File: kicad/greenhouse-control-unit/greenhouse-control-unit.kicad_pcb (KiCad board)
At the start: 2 copper layers, 252.1 x 133.3 mm, 28 parts, among them J1 Screw_Terminal_01x02, J10_Buck2 Conn_01x01_Female, J11_Buck2 Conn_01x01_Female, J12_Buck1 Conn_01x01_Female, J13_Buck1 Conn_01x01_Female, J14_Buck2 Conn_01x01_Female, J15_Buck2 Conn_01x01_Female, J16 Screw_Terminal_01x16, J2 Screw_Terminal_01x02, J3 Screw_Terminal_01x02, J4 Screw_Terminal_01x06, J5 Conn_01x03_Male, J6_Buck1 Conn_01x01_Female, J7_Buck1 Conn_01x01_Female, J8 Conn_01x15_Female, J9 Conn_01x15_Female, Q1 IRLB8721PBF, Q2 IRLB8721PBF, Q3 IRLB8721PBF, Q4 IRLB8721PBF, U1 74HC595, U2 74HC595

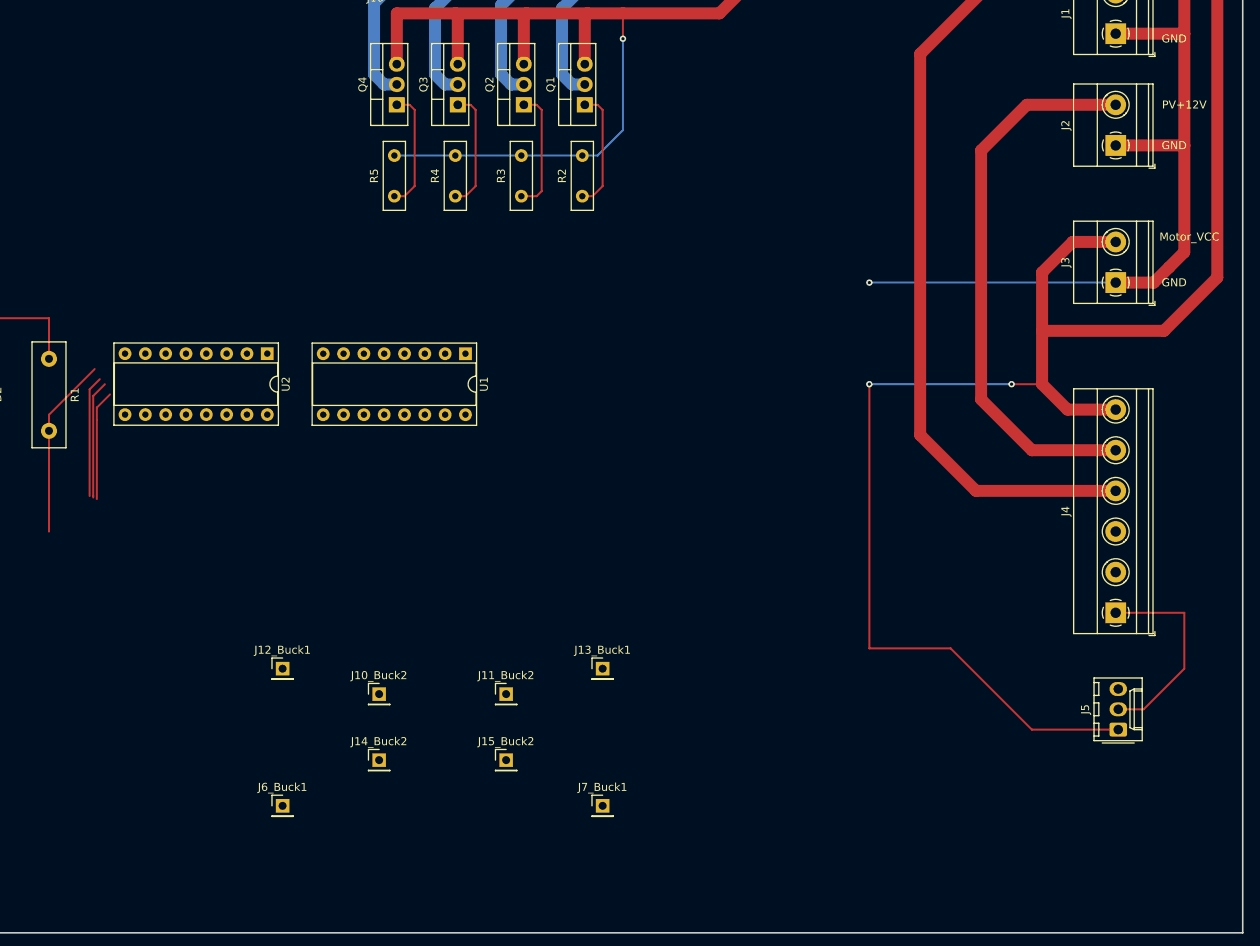
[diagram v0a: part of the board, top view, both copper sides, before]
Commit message: Add SR TTL, FET labels, tie PSU+12V to +12V
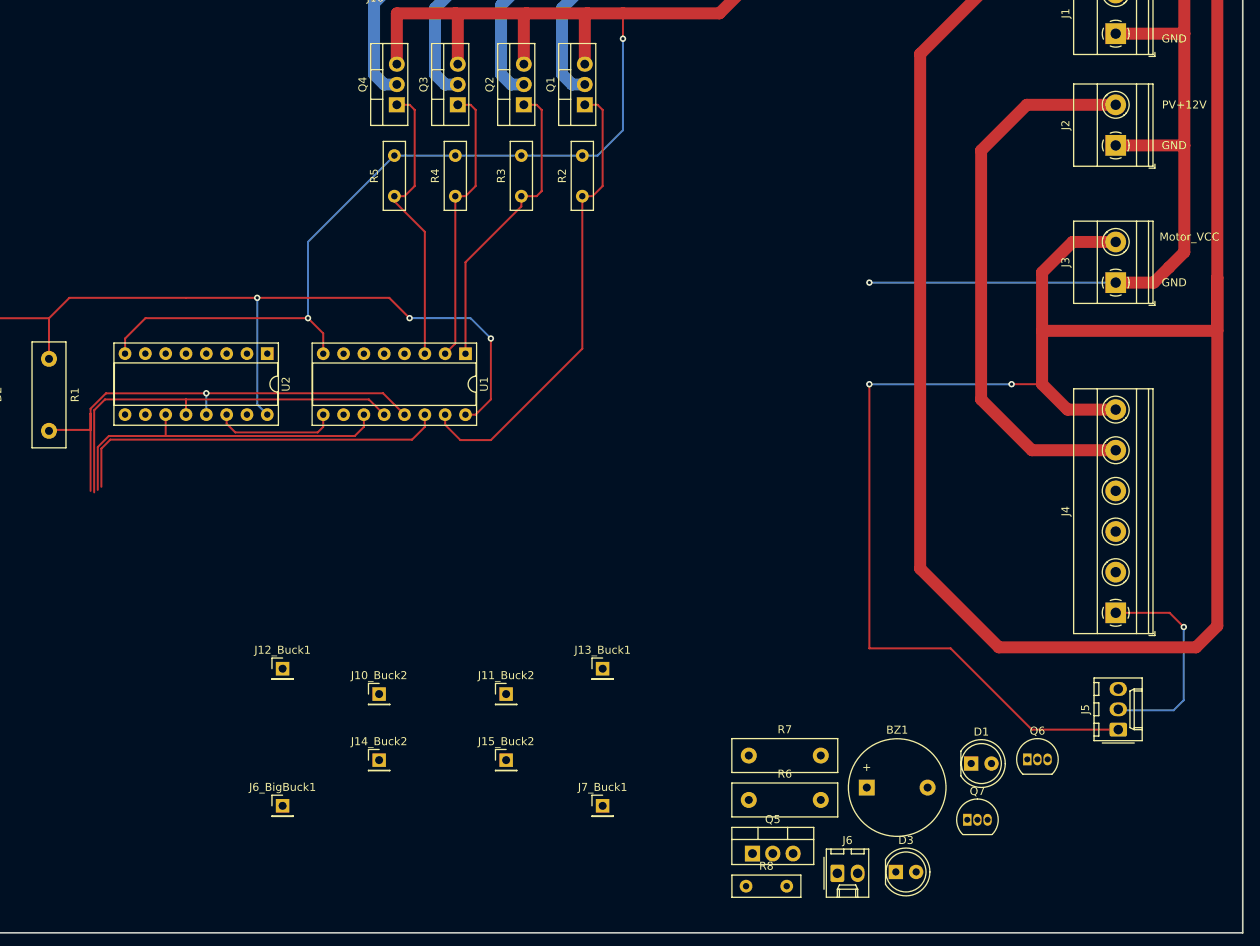
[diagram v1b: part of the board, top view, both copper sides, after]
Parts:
- added BZ1: Buzzer, Buzzer_Beeper:Buzzer_12x9.5RM7.6, F.Cu at (227.3, 137.4)
- added D1: LED, LED_THT:LED_D5.0mm, F.Cu at (240.4, 134.4)
- added D3: LED, LED_THT:LED_D5.0mm, F.Cu at (231.0, 148.0)
- added J6: Conn_01x02_Male, Connector_Molex:Molex_KK-254_AE-6410-02A_1x02_P2.54mm_Vertical, F.Cu at (223.7, 148.1)
- added Q5: IRLB8721PBF, Package_TO_SOT_THT:TO-220-3_Vertical, F.Cu at (213.0, 145.7)
- added Q6: 2N2222A, Package_TO_SOT_THT:TO-92_Inline, F.Cu at (247.4, 133.9)
- added Q7: 2N2222A, Package_TO_SOT_THT:TO-92_Inline, F.Cu at (239.9, 141.4)
- added R6: R4k6, Resistor_THT:R_Box_L13.0mm_W4.0mm_P9.00mm, F.Cu at (212.6, 139.0)
- added R7: R4k6, Resistor_THT:R_Box_L13.0mm_W4.0mm_P9.00mm, F.Cu at (212.6, 133.4)
- added R8: R10k, Resistor_THT:R_Box_L8.4mm_W2.5mm_P5.08mm, F.Cu at (212.2, 149.7)
- renumbered J6_Buck1 to J6_BigBuck1
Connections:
- net /Relay2_IN renamed /ACRelay_IN
- J1 pad 2: /PSU+12V -> +12V
- J4 pad 2: /Relay1_IN -> /FatRelay_Coil
- J4 pad 4: /PSU+12V -> /FatRelay_A
- J9 pad 1: unconnected-(J9-Pad1) -> /MC_D8
- J9 pad 5: /MC_D8 -> unconnected-(J9-Pad5)
- Q1 pad 1: /SR_SW1 -> /SR_SW08
- Q2 pad 1: /SR_SW2 -> /SR_SW09
- Q3 pad 1: /SR_SW3 -> /SR_SW10
- Q4 pad 1: /SR_SW4 -> /SR_SW11
- R2 pad 1: /SR_SW1 -> /SR_SW08
- R3 pad 1: /SR_SW2 -> /SR_SW09
- R4 pad 1: /SR_SW3 -> /SR_SW10
- R5 pad 1: /SR_SW4 -> /SR_SW11
- U1 pad 1: /SR_SW2 -> /StartBeep_SR_SW1
- U1 pad 15: /SR_SW1 -> /FatRelay_SR_SW0
- U1 pad 2: /SR_SW3 -> /CaseFan_SR_SW2
- U1 pad 3: /SR_SW4 -> /SR_SW3
- U1 pad 4: unconnected-(U1-Pad4) -> /SR_SW4
- U1 pad 5: unconnected-(U1-Pad5) -> /SR_SW5
- U1 pad 6: unconnected-(U1-Pad6) -> /SR_SW6
- U1 pad 7: unconnected-(U1-Pad7) -> /SR_SW7
- U2 pad 1: unconnected-(U2-Pad1) -> /SR_SW09
- U2 pad 15: unconnected-(U2-Pad15) -> /SR_SW08
- U2 pad 2: unconnected-(U2-Pad2) -> /SR_SW10
- U2 pad 3: unconnected-(U2-Pad3) -> /SR_SW11
- U2 pad 4: unconnected-(U2-Pad4) -> /SR_SW12
- U2 pad 5: unconnected-(U2-Pad5) -> /SR_SW13
- U2 pad 6: unconnected-(U2-Pad6) -> /SR_SW14
- U2 pad 7: unconnected-(U2-Pad7) -> /SR_SW15
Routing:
- net +12V: track 308.5 -> 490.2 mm
- net /PSU+12V: track 102.6 -> 0.00 mm
- net /SR_VCC: track 17.3 -> 102.4 mm, vias 0 -> 3
- net unconnected-(J9-Pad5): track 0.00 -> 60.8 mm
- net /SR_SW08: track 0.00 -> 58.1 mm
- net GND: track 295.4 -> 353.1 mm, vias 2 -> 4
- net /SR_SW09: track 0.00 -> 38.0 mm
- net /SR_SW11: track 0.00 -> 36.3 mm
- net /MC_D5: track 70.2 -> 106.3 mm
- net /SR_SW10: track 0.00 -> 35.3 mm
- net /MC_D6: track 72.7 -> 105.8 mm
- net /MC_D7: track 74.5 -> 103.2 mm
- net /MC_D8: track 83.5 -> 61.4 mm, vias 0 -> 1
- net Net-(U1-Pad9): track 0.00 -> 15.5 mm
- net /SR_SW2: track 15.5 -> 0.00 mm
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
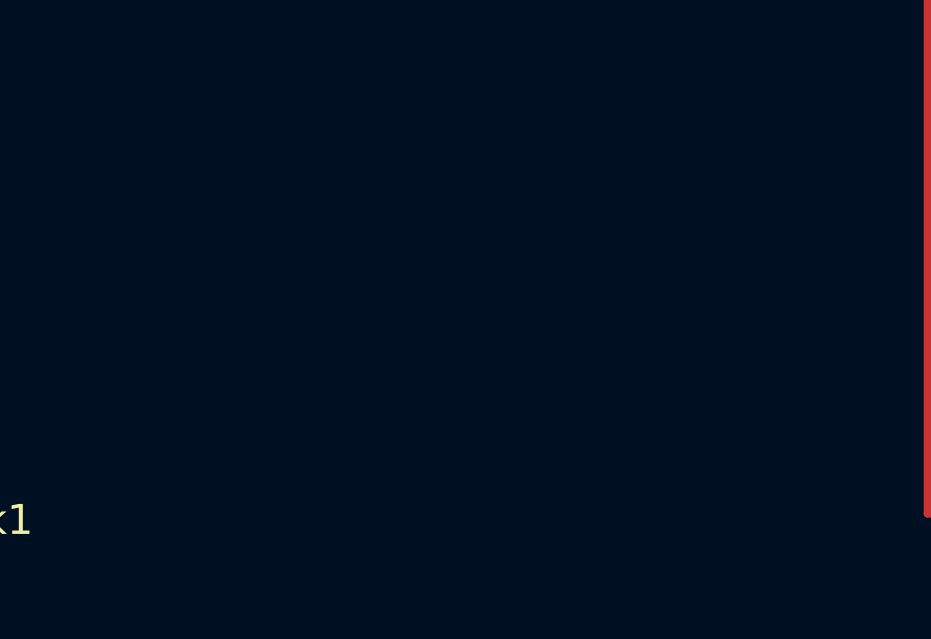
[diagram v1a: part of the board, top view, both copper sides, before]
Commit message: Add LED on when AC PSU relay NC
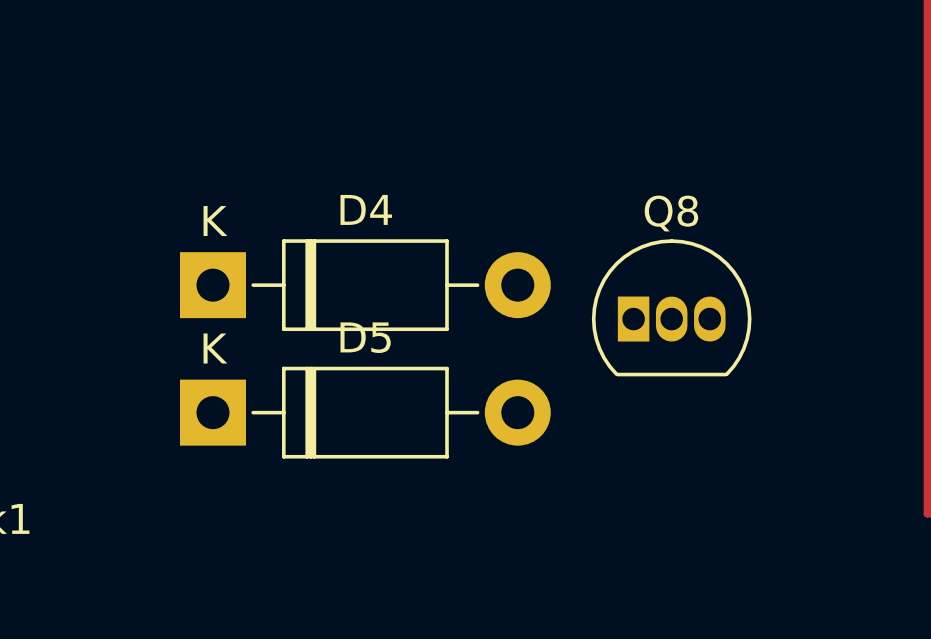
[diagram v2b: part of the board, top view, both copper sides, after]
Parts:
- added D4: 1N4001, Diode_THT:D_DO-41_SOD81_P10.16mm_Horizontal, F.Cu at (203.8, 112.4)
- added D5: 1N4001, Diode_THT:D_DO-41_SOD81_P10.16mm_Horizontal, F.Cu at (203.8, 116.6)
- added Q8: 2N2222A, Package_TO_SOT_THT:TO-92_Inline, F.Cu at (217.9, 113.5)
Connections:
- net /FatRelay_A renamed /BattRelay_A
- net /FatRelay_Coil renamed /BattRelay_Coil
- net /FatRelay_SR_SW0 renamed /BattRelay_SR_SW0
- J5 pad 3: /ACRelay_IN -> /PsuRelay_Coil
- U1 pad 3: /SR_SW3 -> /PsuRelay_SR_SW3

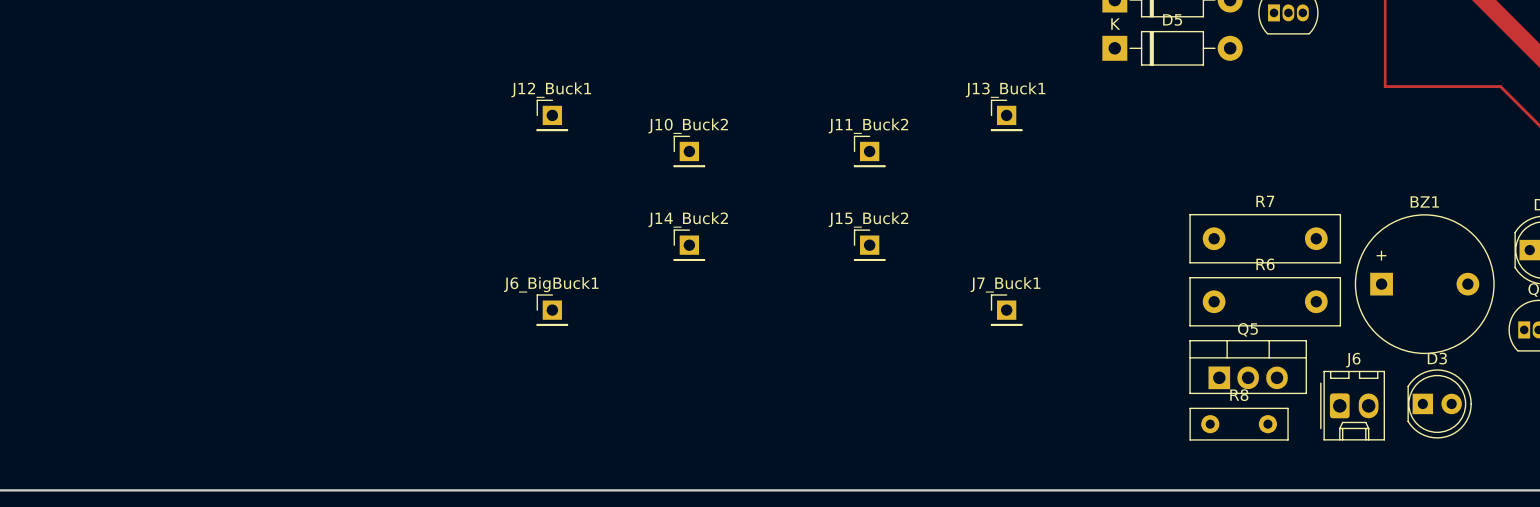
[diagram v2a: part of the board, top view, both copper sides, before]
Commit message: Add battery junction project
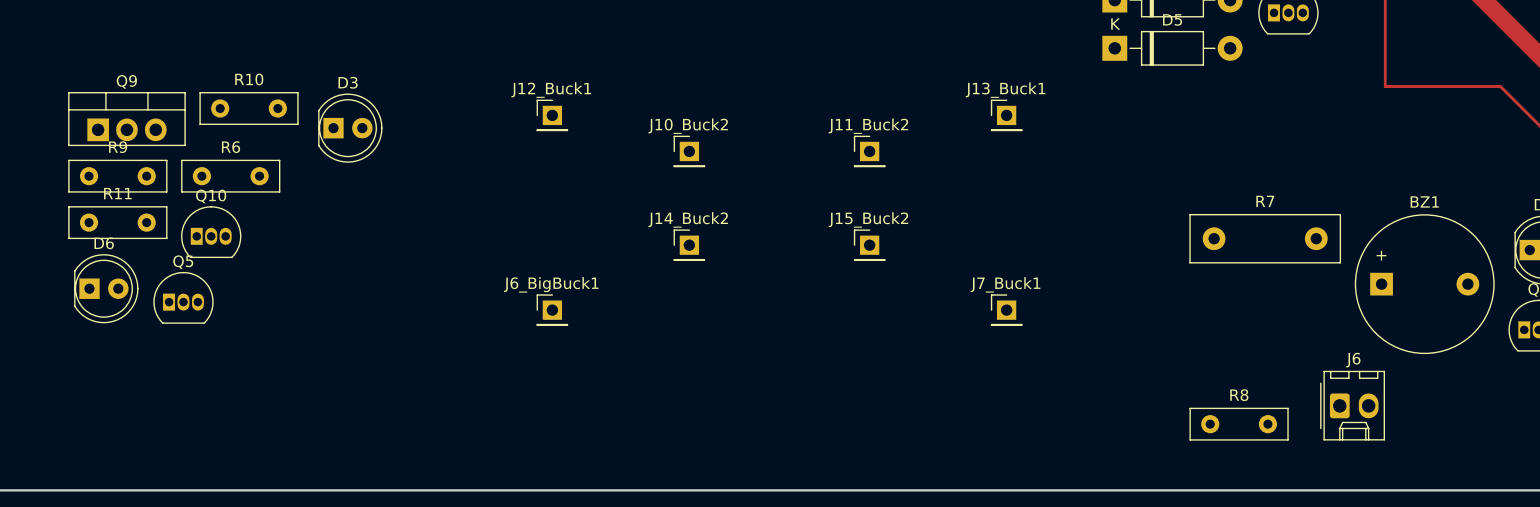
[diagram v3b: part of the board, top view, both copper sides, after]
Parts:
- added D6: LED, LED_THT:LED_D5.0mm, F.Cu at (113.5, 137.8)
- added Q10: 2N2222A, Package_TO_SOT_THT:TO-92_Inline, F.Cu at (123.0, 133.2)
- added Q9: IRLB8721PBF, Package_TO_SOT_THT:TO-220-3_Vertical, F.Cu at (114.3, 123.8)
- added R10: R100, Resistor_THT:R_Box_L8.4mm_W2.5mm_P5.08mm, F.Cu at (125.0, 121.9)
- added R11: 10k, Resistor_THT:R_Box_L8.4mm_W2.5mm_P5.08mm, F.Cu at (113.5, 132.0)
- added R9: 10k, Resistor_THT:R_Box_L8.4mm_W2.5mm_P5.08mm, F.Cu at (113.5, 127.9)
- Q5: value IRLB8721PBF -> 2N2222A; footprint Package_TO_SOT_THT:TO-220-3_Vertical -> Package_TO_SOT_THT:TO-92_Inline
- R6: value R4k6 -> R100; footprint Resistor_THT:R_Box_L13.0mm_W4.0mm_P9.00mm -> Resistor_THT:R_Box_L8.4mm_W2.5mm_P5.08mm
- moved D3 99.0 mm to (135.0, 123.7)
- moved Q5 92.7 mm to (120.5, 139.0)
- moved R6 89.8 mm to (123.4, 127.9)
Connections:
- net /PsuRelay_Coil renamed /PsuRelayNC_Coil
- D3 pad 1: Net-(D3-Pad1) -> GND
- D3 pad 2: /BattRelay_SR_SW0 -> Net-(D3-Pad2)
- Q5 pad 1: /BattRelay_SR_SW0 -> GND
- Q5 pad 2: /BattRelay_Coil -> Net-(Q5-Pad2)
- Q5 pad 3: GND -> Net-(D3-Pad2)
- Q8 pad 2: /PsuRelay_SR_SW3 -> /PsuRelayNC_SR_SW3
- R6 pad 1: Net-(D3-Pad1) -> /PsuRelayNC_SR_SW3
- R6 pad 2: GND -> Net-(Q5-Pad2)
- U1 pad 3: /PsuRelay_SR_SW3 -> /PsuRelayNC_SR_SW3

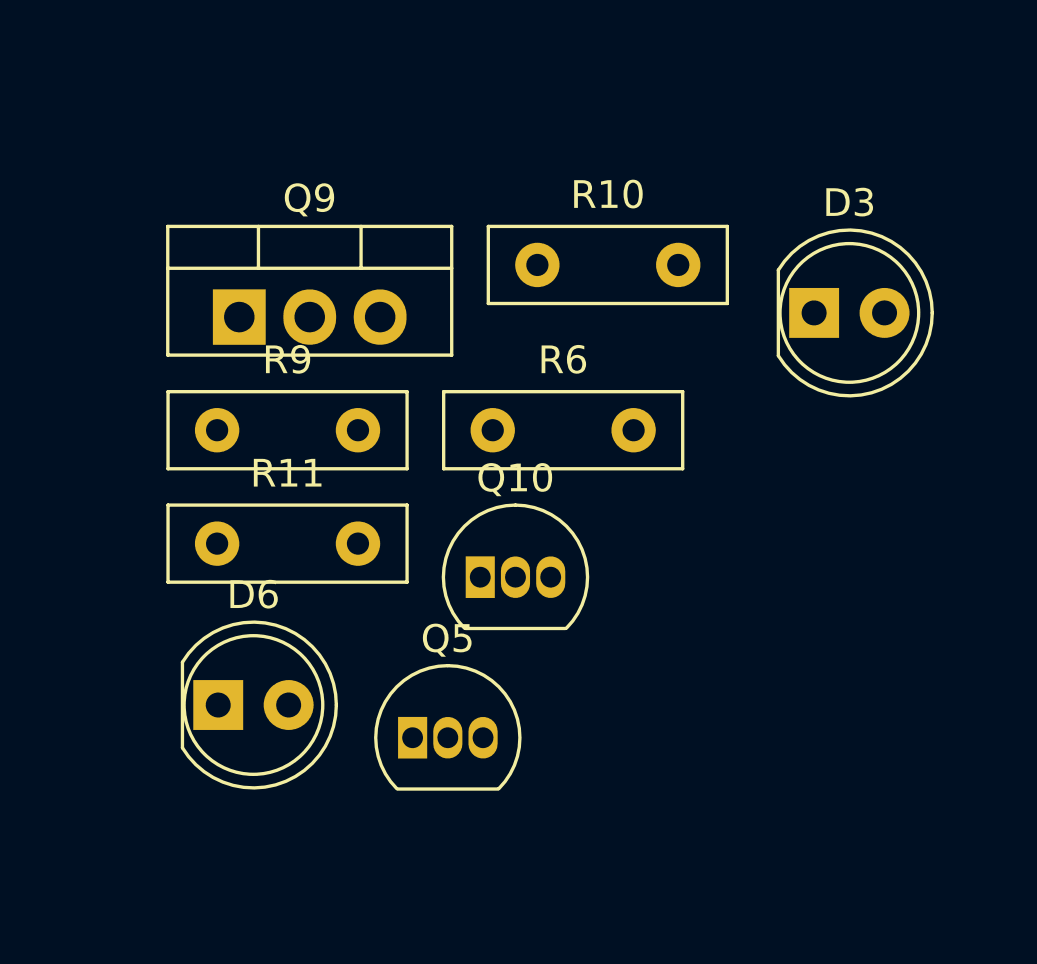
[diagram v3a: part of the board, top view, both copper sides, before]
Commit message: Moved power source LEDs to SR, changed label names
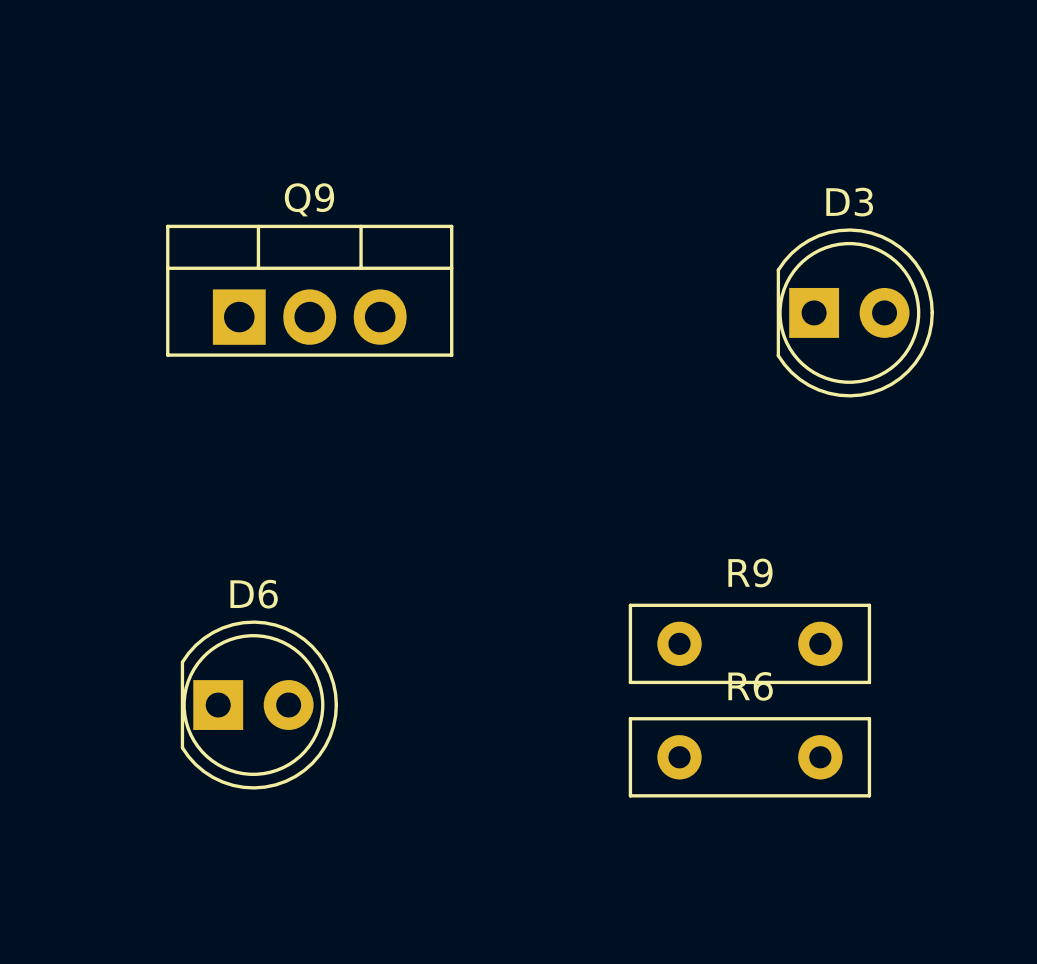
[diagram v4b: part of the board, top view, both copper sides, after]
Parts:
- removed Q10, Q5: 2N2222A, Package_TO_SOT_THT:TO-92_Inline
- removed R10: R100, Resistor_THT:R_Box_L8.4mm_W2.5mm_P5.08mm
- removed R11: 10k, Resistor_THT:R_Box_L8.4mm_W2.5mm_P5.08mm
- R6: value R100 -> 10k
- moved R9 18.4 mm to (130.2, 135.6)
- moved R6 13.6 mm to (130.2, 139.7)
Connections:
- net /BattRelay_A renamed /BattRelayNC_A
- net /BattRelay_Coil renamed /BattRelayNC_Coil
- net /BattRelay_SR_SW0 renamed /BattRelayNC_SR_Q0
- net /CaseFan_SR_SW2 renamed /CaseFan_SR_Q2
- net /SR_SW08 renamed /SW1_SR_Q08
- net /SR_SW09 renamed /SW2_SR_Q09
- net /SR_SW10 renamed /SW3_SR_Q10
- net /SR_SW11 renamed /SW4_SR_Q11
- net /SR_SW12 renamed /SR_Q12
- net /SR_SW13 renamed /SR_Q13
- net /SR_SW14 renamed /SR_Q14
- net /SR_SW15 renamed /SR_Q15
- net /SR_SW6 renamed /SR_Q6
- net /SR_SW7 renamed /SR_Q7
- net /StartBeep_SR_SW1 renamed /StartBeep_SR_Q1
- Q8 pad 2: /PsuRelayNC_SR_SW3 -> /PsuRelayNC_SR_Q3
- R6 pad 1: /PsuRelayNC_SR_SW3 -> /BatteryLed_SR_Q4
- R6 pad 2: Net-(Q5-Pad2) -> Net-(D6-Pad2)
- R9 pad 1: +5V -> /PsuLed_SR_Q5
- U1 pad 3: /PsuRelayNC_SR_SW3 -> /PsuRelayNC_SR_Q3
- U1 pad 4: /SR_SW4 -> /BatteryLed_SR_Q4
- U1 pad 5: /SR_SW5 -> /PsuLed_SR_Q5
